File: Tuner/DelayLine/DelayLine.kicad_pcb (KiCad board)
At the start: 2 copper layers, 100 x 100 mm, 85 parts, among them J1 Conn_Coaxial, J10 Conn_Coaxial, J11 Conn_Coaxial, J12 Conn_Coaxial, J13 Conn_01x01, J14 Conn_01x01, J15 Conn_01x01, J16 Conn_01x01, J17 Conn_02x10_Odd_Even, J18 Conn_Coaxial, J19 Conn_Coaxial, J20 Conn_Coaxial, J21 Conn_Coaxial, J22 Conn_Coaxial, J23 Conn_Coaxial, J24 Conn_01x01, J25 Conn_01x01, J26 Conn_01x01, J27 Conn_01x01, J28 Conn_01x01, J29 Conn_Coaxial, J3 Conn_Coaxial, J31 Conn_Coaxial, J32 Conn_01x01, J33 Conn_01x01, J34 Conn_01x01, J35 Conn_01x01, J5 Conn_Coaxial, J6 Conn_Coaxial, J7 Conn_Coaxial, J8 Conn_01x02, J9 Conn_01x02

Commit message: Stupid mistake, went to another method
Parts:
- moved J19 3.63 mm to (116.6, 107.1)
- moved J6 2.70 mm to (124.1, 119.0)
- moved J12 2.59 mm to (108.6, 119.3)
- moved J10 2.48 mm to (131.8, 106.8)
- moved J23 2.46 mm to (100.0, 106.8)
- moved J29 1.78 mm to (75.1, 119.0)
- moved J21 1.75 mm to (92.0, 119.1)
- moved J31 1.63 mm to (83.5, 106.9)
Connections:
- J22 pad 1: Net-(J11-Pad1) -> Net-(J22-Pad1)
- J23 pad 1: Net-(J12-Pad1) -> Net-(J23-Pad1)
- J24 pad 1: Net-(J20-Pad1) -> Net-(J24-Pad1)
- J3 pad 1: Net-(J29-Pad1) -> Net-(J3-Pad1)
- J31 pad 1: Net-(J21-Pad1) -> Net-(J31-Pad1)
- J5 pad 1: Net-(J18-Pad1) -> Net-(J5-Pad1)
- J6 pad 1: Net-(J19-Pad1) -> Net-(J6-Pad1)
- J7 pad 1: Net-(J1-Pad1) -> Net-(J7-Pad1)
- RLY1 pad 4: Net-(J10-Pad1) -> Net-(RLY1-Pad4)
- RLY1 pad 8: Net-(J10-Pad1) -> Net-(RLY1-Pad4)
- RLY10 pad 3: Net-(J20-Pad1) -> Net-(J24-Pad1)
- RLY10 pad 7: Net-(J20-Pad1) -> (no net)
- RLY2 pad 2: Net-(J10-Pad1) -> Net-(RLY2-Pad2)
- RLY2 pad 3: Net-(J19-Pad1) -> Net-(RLY2-Pad3)
- RLY2 pad 4: (no net) -> Net-(J6-Pad1)
- RLY2 pad 6: Net-(J10-Pad1) -> Net-(RLY1-Pad4)
- RLY2 pad 7: Net-(J19-Pad1) -> Net-(RLY2-Pad3)
- RLY2 pad 8: (no net) -> Net-(J10-Pad1)
- RLY3 pad 2: Net-(J19-Pad1) -> Net-(RLY3-Pad2)
- RLY3 pad 3: Net-(J12-Pad1) -> Net-(RLY3-Pad3)
- RLY3 pad 4: (no net) -> Net-(J12-Pad1)
- RLY3 pad 6: Net-(J19-Pad1) -> Net-(RLY2-Pad2)
- RLY3 pad 7: Net-(J12-Pad1) -> Net-(RLY3-Pad3)
- RLY3 pad 8: (no net) -> Net-(J19-Pad1)
- RLY4 pad 2: Net-(J12-Pad1) -> Net-(RLY4-Pad2)
- RLY4 pad 3: Net-(J21-Pad1) -> Net-(RLY4-Pad3)
- RLY4 pad 4: (no net) -> Net-(J21-Pad1)
- RLY4 pad 6: Net-(J12-Pad1) -> Net-(RLY3-Pad2)
- RLY4 pad 7: Net-(J21-Pad1) -> Net-(RLY4-Pad3)
- RLY4 pad 8: (no net) -> Net-(J23-Pad1)
- RLY5 pad 2: Net-(J21-Pad1) -> Net-(RLY5-Pad2)
- RLY5 pad 3: Net-(J29-Pad1) -> Net-(RLY5-Pad3)
- RLY5 pad 4: (no net) -> Net-(J29-Pad1)
- RLY5 pad 6: Net-(J21-Pad1) -> Net-(RLY4-Pad2)
- RLY5 pad 7: Net-(J29-Pad1) -> Net-(RLY5-Pad3)
- RLY5 pad 8: (no net) -> Net-(J31-Pad1)
- RLY6 pad 2: Net-(J29-Pad1) -> Net-(RLY6-Pad2)
- RLY6 pad 3: Net-(J1-Pad1) -> Net-(RLY6-Pad3)
- RLY6 pad 4: (no net) -> Net-(J1-Pad1)
- RLY6 pad 6: Net-(J29-Pad1) -> Net-(RLY5-Pad2)
- RLY6 pad 7: Net-(J1-Pad1) -> Net-(RLY6-Pad3)
- RLY6 pad 8: (no net) -> Net-(J3-Pad1)
- RLY7 pad 2: Net-(J1-Pad1) -> Net-(RLY7-Pad2)
- RLY7 pad 3: Net-(J18-Pad1) -> Net-(RLY7-Pad3)
- RLY7 pad 4: (no net) -> Net-(J5-Pad1)
- RLY7 pad 6: Net-(J1-Pad1) -> Net-(RLY6-Pad2)
- RLY7 pad 7: Net-(J18-Pad1) -> Net-(RLY7-Pad3)
- RLY7 pad 8: (no net) -> Net-(J7-Pad1)
- RLY8 pad 2: Net-(J18-Pad1) -> Net-(RLY8-Pad2)
- RLY8 pad 3: Net-(J11-Pad1) -> Net-(RLY8-Pad3)
- RLY8 pad 4: (no net) -> Net-(J11-Pad1)
- RLY8 pad 6: Net-(J18-Pad1) -> Net-(RLY7-Pad2)
- RLY8 pad 7: Net-(J11-Pad1) -> Net-(RLY8-Pad3)
- RLY8 pad 8: (no net) -> Net-(J18-Pad1)
- RLY9 pad 2: Net-(J11-Pad1) -> Net-(J24-Pad1)
- RLY9 pad 3: Net-(J20-Pad1) -> Net-(RLY9-Pad3)
- RLY9 pad 4: (no net) -> Net-(J20-Pad1)
- RLY9 pad 6: Net-(J11-Pad1) -> Net-(RLY8-Pad2)
- RLY9 pad 7: Net-(J20-Pad1) -> Net-(RLY9-Pad3)
- RLY9 pad 8: (no net) -> Net-(J22-Pad1)
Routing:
- net Net-(RLY5-Pad2): track 0.00 -> 79.9 mm
- net Net-(J29-Pad1): track 91.4 -> 12.5 mm
- net Net-(J1-Pad1): track 62.0 -> 8.69 mm
- net Net-(J11-Pad1): track 62.9 -> 9.88 mm
- net RFGND: track 906.3 -> 854.0 mm
- net Net-(J21-Pad1): track 60.1 -> 13.0 mm
- net Net-(J12-Pad1): track 58.6 -> 13.4 mm
- net Net-(J20-Pad1): track 53.3 -> 10.5 mm
- net Net-(J18-Pad1): track 62.7 -> 23.5 mm
- net Net-(J24-Pad1): track 0.00 -> 38.2 mm
- net Net-(J19-Pad1): track 59.0 -> 25.1 mm
- net Net-(J10-Pad1): track 49.5 -> 24.6 mm
- net Net-(J31-Pad1): track 0.00 -> 23.9 mm
- net Net-(J22-Pad1): track 0.00 -> 23.8 mm
- net Net-(J7-Pad1): track 0.00 -> 23.7 mm
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
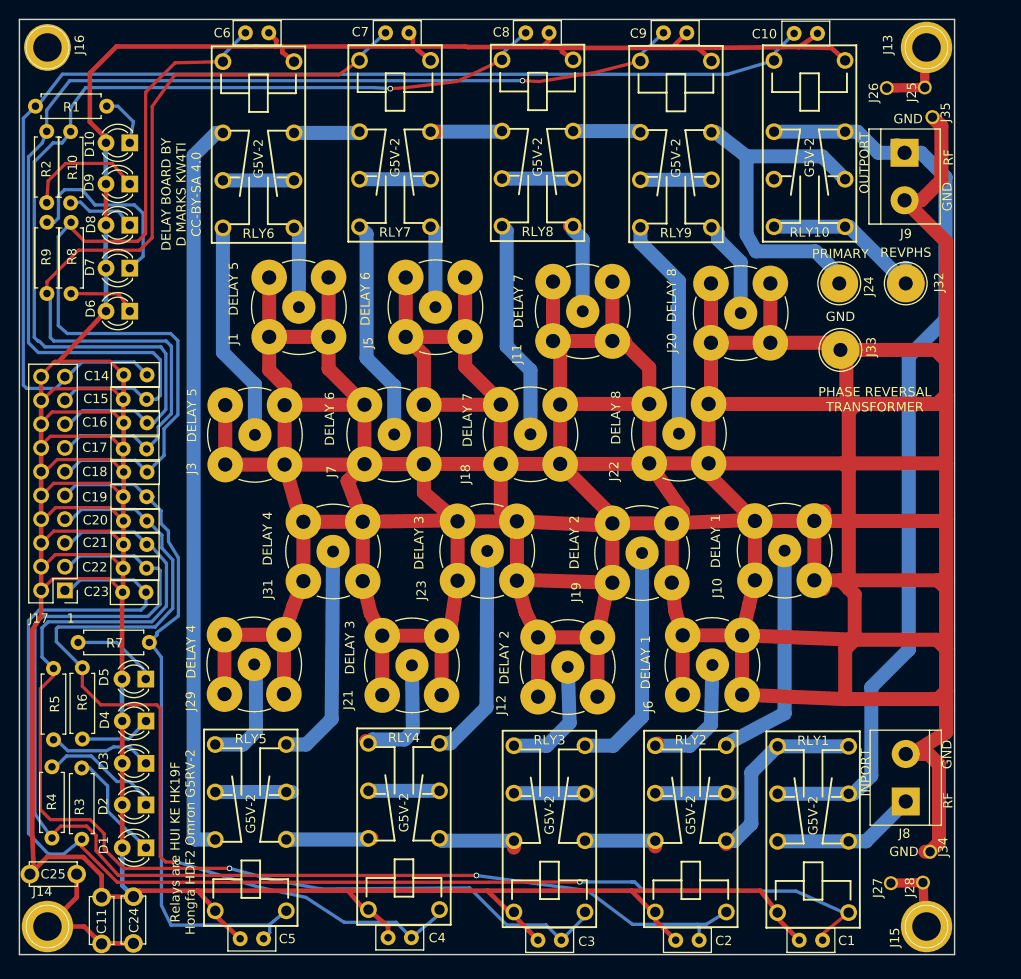
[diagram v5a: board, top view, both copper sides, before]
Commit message: Added LittleDelayLine
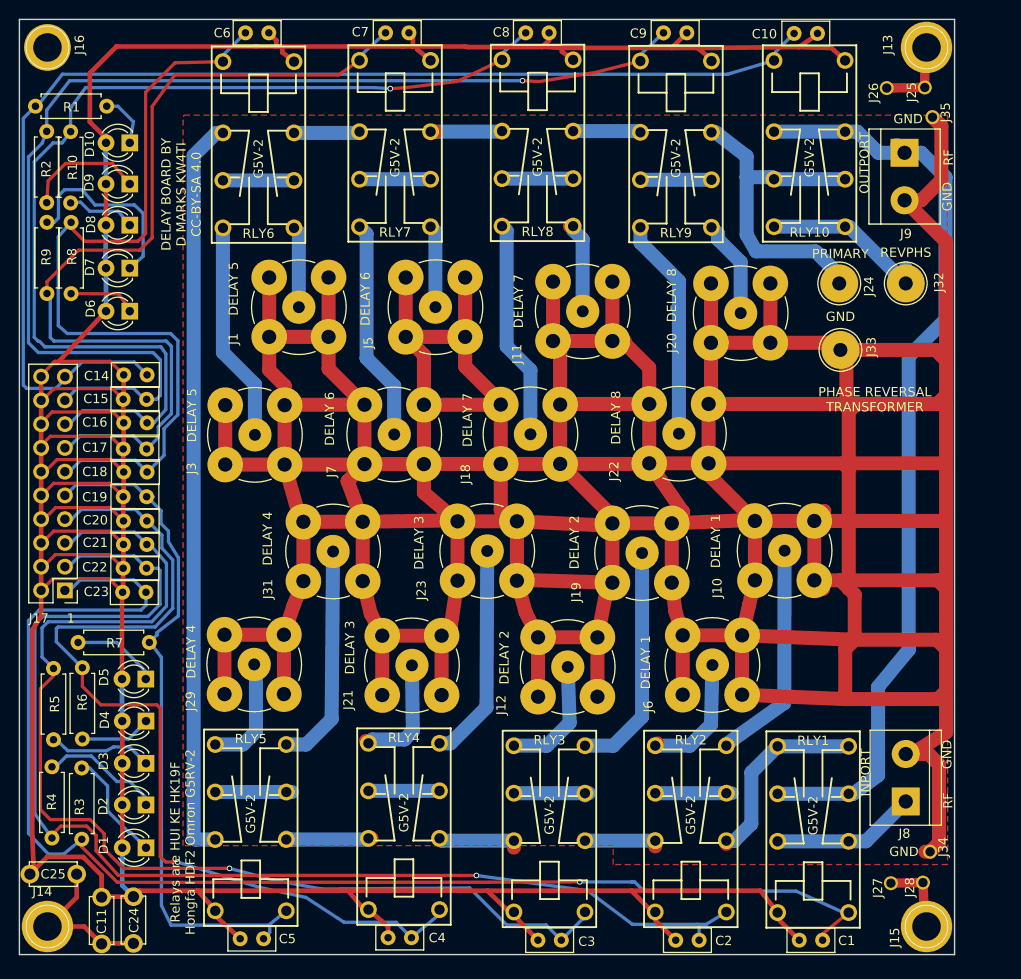
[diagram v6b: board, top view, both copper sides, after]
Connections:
- RLY10 pad 7: (no net) -> Net-(J24-Pad1)
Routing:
- net Net-(J24-Pad1): track 38.2 -> 37.3 mm
- net Net-(J10-Pad1): track 24.6 -> 24.0 mm
- added copper zone on F.Cu, net RFGND
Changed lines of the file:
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@@
 (kicad_pcb (version 4) (host pcbnew 4.0.7)
   (general
-    (links 220)
+    (links 221)
     (no_connects 0)
-    (area 49.924999 49.924999 150.075001 150.075001)
+    (area 44.941618 49.609999 151.74762 151.075)
     (thickness 1.6)
     (drawings 35)
-    (tracks 907)
+    (tracks 909)
     (zones 0)
     (modules 85)
@@
     (user_trace_width 1.5)
     (trace_clearance 0.2)
-    (zone_clearance 1.5)
+    (zone_clearance 1)
     (zone_45_only yes)
     (trace_min 0.2)
@@
     (pad 3 thru_hole circle (at 10.32 -3.8 270) (size 1.8 1.8) (drill 1.1) (layers *.Cu *.Mask)
       (net 52 "Net-(J24-Pad1)"))
-    (pad 7 thru_hole circle (at 10.32 3.8 270) (size 1.8 1.8) (drill 1.1) (layers *.Cu *.Mask))
+    (pad 7 thru_hole circle (at 10.32 3.8 270) (size 1.8 1.8) (drill 1.1) (layers *.Cu *.Mask)
+      (net 52 "Net-(J24-Pad1)"))
     (pad 6 thru_hole circle (at 5.24 3.8 270) (size 1.8 1.8) (drill 1.1) (layers *.Cu *.Mask)
       (net 37 RFOUT))
@@
   (segment (start 79.883 72.814) (end 79.365 72.296) (width 1.5) (layer B.Cu) (net 2))
   (segment (start 125.593 127.6655) (end 125.593 127.518) (width 1.5) (layer B.Cu) (net 3))
-  (segment (start 125.593 127.518) (end 131.826 124.2187) (width 1.5) (layer B.Cu) (net 3))
-  (segment (start 131.826 124.2187) (end 131.826 106.807) (width 1.5) (layer B.Cu) (net 3) (status 20))
+  (segment (start 125.593 127.518) (end 131.7879 123.1011) (width 1.5) (layer B.Cu) (net 3))
+  (segment (start 131.7879 123.1011) (end 131.826 106.807) (width 1.5) (layer B.Cu) (net 3) (status 800020))
   (segment (start 115.481152 142.237678) (end 115.796278 142.237678) (width 0.35) (layer B.Cu) (net 4))
   (segment (start 116.7765 143.2179) (end 133.056967 143.2179) (width 0.35) (layer B.Cu) (net 4))
@@
   (segment (start 138.674 132.809) (end 131.074 132.809) (width 1.5) (layer B.Cu) (net 37))
   (segment (start 138.674 132.809) (end 139.1615 132.809) (width 1.5) (layer B.Cu) (net 37))
-  (segment (start 139.1615 132.809) (end 141.097 130.8735) (width 1.5) (layer B.Cu) (net 37))
-  (segment (start 141.097 130.8735) (end 141.097 121.412) (width 1.5) (layer B.Cu) (net 37))
-  (segment (start 141.097 121.412) (end 145.0975 117.4115) (width 1.5) (layer B.Cu) (net 37))
+  (segment (start 139.1615 132.809) (end 141.8209 130.8481) (width 1.5) (layer B.Cu) (net 37))
+  (segment (start 141.8209 130.8481) (end 141.8209 121.3866) (width 1.5) (layer B.Cu) (net 37))
+  (segment (start 141.8209 121.3866) (end 145.0975 117.4115) (width 1.5) (layer B.Cu) (net 37))
   (segment (start 145.0975 117.4115) (end 145.0975 86.0425) (width 1.5) (layer B.Cu) (net 37))
   (segment (start 145.0975 86.0425) (end 149.0345 82.1055) (width 1.5) (layer B.Cu) (net 37))
@@
   (segment (start 94.488 80.772) (end 94.488 72.687) (width 1.5) (layer B.Cu) (net 51))
   (segment (start 94.488 72.687) (end 93.97 72.169) (width 1.5) (layer B.Cu) (net 51))
+  (segment (start 127.762 66.8655) (end 130.4695 66.8655) (width 1.5) (layer B.Cu) (net 52))
+  (segment (start 130.4695 66.8655) (end 130.693 67.089) (width 1.5) (layer B.Cu) (net 52))
+  (segment (start 138.293 67.089) (end 130.693 67.089) (width 1.5) (layer B.Cu) (net 52))
   (segment (start 137.668 78.232) (end 137.668 77.343) (width 1.5) (layer B.Cu) (net 52))
   (segment (start 137.668 77.343) (end 135.128 74.803) (width 1.5) (layer B.Cu) (net 52))
-  (segment (start 127.762 73.025) (end 127.762 64.643) (width 1.5) (layer B.Cu) (net 52))
+  (segment (start 127.762 73.025) (end 127.762 66.8655) (width 1.5) (layer B.Cu) (net 52))
+  (segment (start 127.762 66.8655) (end 127.762 64.643) (width 1.5) (layer B.Cu) (net 52))
   (segment (start 128.778 74.803) (end 127.762 73.025) (width 1.5) (layer B.Cu) (net 52))
   (segment (start 135.128 74.803) (end 128.778 74.803) (width 1.5) (layer B.Cu) (net 52))
   (segment (start 124.0055 62.0725) (end 124.4295 62.0725) (width 1.5) (layer B.Cu) (net 52))
   (segment (start 124.4295 62.0725) (end 127.762 64.643) (width 1.5) (layer B.Cu) (net 52))
-  (segment (start 135.847 64.643) (end 138.293 67.089) (width 1.5) (layer B.Cu) (net 52))
-  (segment (start 127.762 64.643) (end 135.847 64.643) (width 1.5) (layer B.Cu) (net 52))
   (segment (start 124.0055 62.0725) (end 124.2365 62.0725) (width 1.5) (layer F.Cu) (net 52))
   (segment (start 137.668 78.232) (end 137.668 77.851) (width 1.5) (layer B.Cu) (net 52))
@@
   (segment (start 123.952 119.1895) (end 124.1044 119.0371) (width 1.5) (layer B.Cu) (net 61) (status 30))
   (segment (start 118.237 127.4215) (end 117.993 127.6655) (width 1.5) (layer F.Cu) (net 61))
+  (zone (net 1) (net_name RFGND) (layer F.Cu) (hatch edge 0.508)
+    (connect_pads (clearance 1))
+    (min_thickness 0.635)
+    (fill yes (arc_segments 16) (thermal_gap 0.508) (thermal_bridge_width 3))
+    (polygon
+      (pts
+        (xy 67.6148 60.2361) (xy 149.2504 60.2361) (xy 149.2504 140.3731) (xy 113.4872 140.3731) (xy 113.4872 138.3538)
+        (xy 67.5005 138.3538) (xy 67.5005 60.3504) (xy 67.6148 60.3504)
+      )
+    )
+  )
 )

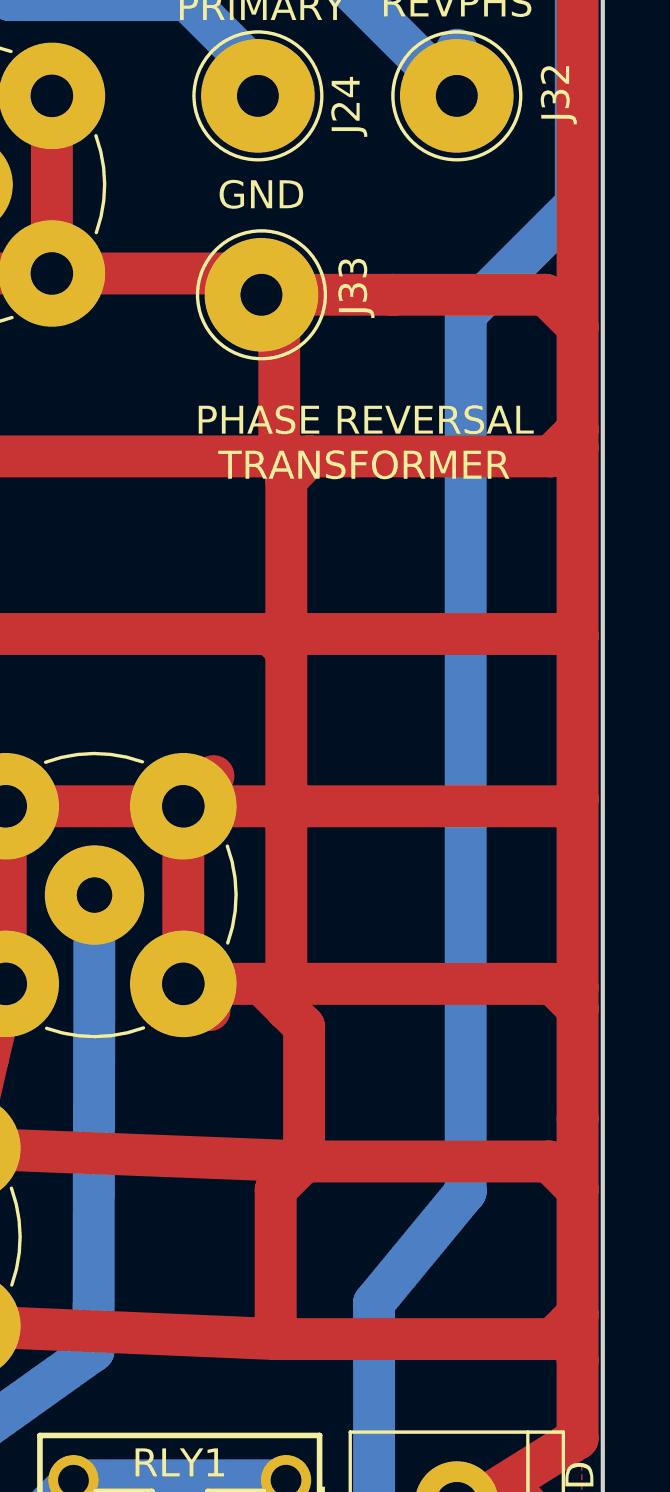
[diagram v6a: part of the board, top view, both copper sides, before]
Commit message: Added more instrumentation to TandemMatch, fixed grounding issue
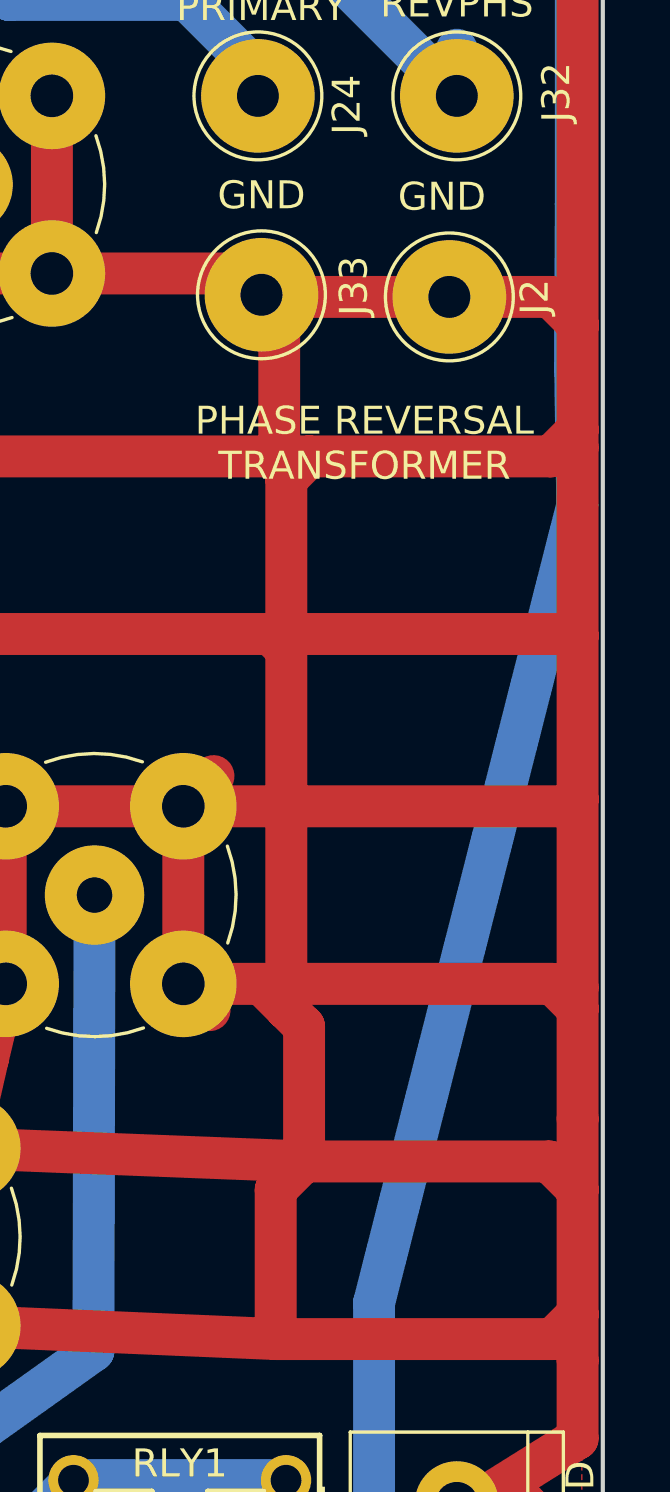
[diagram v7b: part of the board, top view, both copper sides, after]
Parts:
- added J2: Conn_01x01, Connectors:1pin, F.Cu at (144.5, 85.4)
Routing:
- net RFOUT: track 99.7 -> 97.8 mm
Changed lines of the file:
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@@
 (kicad_pcb (version 4) (host pcbnew 4.0.7)
   (general
-    (links 221)
+    (links 222)
     (no_connects 0)
-    (area 44.941618 49.609999 151.74762 151.075)
+    (area 49.924999 49.924999 150.075001 150.075001)
     (thickness 1.6)
-    (drawings 35)
-    (tracks 909)
+    (drawings 36)
+    (tracks 911)
     (zones 0)
-    (modules 85)
+    (modules 86)
     (nets 62)
   )
@@
       (net 1 RFGND))
   )
+  (module Connectors:1pin (layer F.Cu)
+    (at 144.5133 85.4202 270)
+    (descr "module 1 pin (ou trou mecanique de percage)")
+    (tags DEV)
+    (fp_text reference J2 (at 0 -3.048 270) (layer F.SilkS)
+      (effects (font (size 1 1) (thickness 0.15)))
+    )
+    (fp_text value Conn_01x01 (at 0 3 270) (layer F.Fab)
+      (effects (font (size 1 1) (thickness 0.15)))
+    )
+    (fp_circle (center 0 0) (end 2 0.8) (layer F.Fab) (width 0.1))
+    (fp_circle (center 0 0) (end 2.6 0) (layer F.CrtYd) (width 0.05))
+    (fp_circle (center 0 0) (end 0 -2.286) (layer F.SilkS) (width 0.12))
+    (pad 1 thru_hole circle (at 0 0 270) (size 4.064 4.064) (drill 1.5) (layers *.Cu *.Mask)
+      (net 1 RFGND))
+  )
+  (gr_text GND (at 144.2466 81.8388) (layer F.SilkS)
+    (effects (font (size 1 1) (thickness 0.15)))
+  )
   (gr_text GND (at 144.5895 139.0015) (layer F.SilkS)
     (effects (font (size 1 1) (thickness 0.15)))
@@
   (gr_line (start 150 150) (end 50 150) (angle 90) (layer Edge.Cuts) (width 0.15))
   (gr_line (start 50 50) (end 150 50) (angle 90) (layer Edge.Cuts) (width 0.15))
+  (segment (start 144.5133 85.4202) (end 148.1328 85.4202) (width 1.5) (layer F.Cu) (net 1))
+  (segment (start 148.1328 85.4202) (end 149.098 86.3854) (width 1.5) (layer F.Cu) (net 1))
+  (segment (start 144.5133 85.4202) (end 137.8712 85.4202) (width 1.5) (layer F.Cu) (net 1))
+  (segment (start 137.8712 85.4202) (end 137.795 85.344) (width 1.5) (layer F.Cu) (net 1))
   (segment (start 138.43 91.1225) (end 138.43 85.979) (width 1.5) (layer F.Cu) (net 1))
   (segment (start 138.43 85.979) (end 137.795 85.344) (width 1.5) (layer F.Cu) (net 1))
@@
   (segment (start 148.336 129.667) (end 148.336 138.049) (width 1.5) (layer F.Cu) (net 1))
   (segment (start 147.2184 128.5494) (end 148.336 129.667) (width 1.5) (layer F.Cu) (net 1))
-  (segment (start 137.795 85.344) (end 142.494 85.344) (width 1.5) (layer F.Cu) (net 1))
-  (segment (start 142.494 85.344) (end 147.955 85.344) (width 1.5) (layer F.Cu) (net 1))
-  (segment (start 147.955 85.344) (end 149.098 86.487) (width 1.5) (layer F.Cu) (net 1))
   (segment (start 144.78 128.5494) (end 145.4023 128.5494) (width 1.5) (layer F.Cu) (net 1) (status 30))
   (segment (start 145.4023 128.5494) (end 149.098 126.238) (width 1.5) (layer F.Cu) (net 1) (status 10))
@@
   (segment (start 149.098 97.536) (end 149.098 90.805) (width 1.5) (layer F.Cu) (net 1))
   (segment (start 149.098 90.805) (end 149.098 90.17) (width 1.5) (layer F.Cu) (net 1))
-  (segment (start 149.098 90.17) (end 149.098 86.487) (width 1.5) (layer F.Cu) (net 1))
-  (segment (start 149.098 73.787) (end 144.653 69.342) (width 1.5) (layer F.Cu) (net 1))
+  (segment (start 149.098 90.17) (end 149.098 86.3854) (width 1.5) (layer F.Cu) (net 1))
+  (segment (start 149.098 86.3854) (end 149.098 86.487) (width 1.5) (layer F.Cu) (net 1))
   (segment (start 149.098 86.487) (end 149.098 73.787) (width 1.5) (layer F.Cu) (net 1))
+  (segment (start 149.098 73.787) (end 144.653 69.342) (width 1.5) (layer F.Cu) (net 1))
   (segment (start 144.78 128.5494) (end 145.3896 128.5494) (width 1) (layer F.Cu) (net 1) (status 30))
   (segment (start 145.39468 70.08368) (end 144.653 69.342) (width 1.5) (layer F.Cu) (net 1) (status 30))
@@
   (segment (start 125.593 127.6655) (end 125.593 127.518) (width 1.5) (layer B.Cu) (net 3))
   (segment (start 125.593 127.518) (end 131.7879 123.1011) (width 1.5) (layer B.Cu) (net 3))
-  (segment (start 131.7879 123.1011) (end 131.826 106.807) (width 1.5) (layer B.Cu) (net 3) (status 800020))
+  (segment (start 131.7879 123.1011) (end 131.826 106.807) (width 1.5) (layer B.Cu) (net 3) (status 20))
   (segment (start 115.481152 142.237678) (end 115.796278 142.237678) (width 0.35) (layer B.Cu) (net 4))
   (segment (start 116.7765 143.2179) (end 133.056967 143.2179) (width 0.35) (layer B.Cu) (net 4))
@@
   (segment (start 139.1615 132.809) (end 141.8209 130.8481) (width 1.5) (layer B.Cu) (net 37))
   (segment (start 141.8209 130.8481) (end 141.8209 121.3866) (width 1.5) (layer B.Cu) (net 37))
-  (segment (start 141.8209 121.3866) (end 145.0975 117.4115) (width 1.5) (layer B.Cu) (net 37))
-  (segment (start 145.0975 117.4115) (end 145.0975 86.0425) (width 1.5) (layer B.Cu) (net 37))
-  (segment (start 145.0975 86.0425) (end 149.0345 82.1055) (width 1.5) (layer B.Cu) (net 37))
+  (segment (start 141.8209 121.3866) (end 149.08784 92.87256) (width 1.5) (layer B.Cu) (net 37))
+  (segment (start 149.08784 92.87256) (end 149.0091 87.94242) (width 1.5) (layer B.Cu) (net 37))
+  (segment (start 149.0091 87.94242) (end 149.0345 82.1055) (width 1.5) (layer B.Cu) (net 37))
   (segment (start 149.0345 82.1055) (end 149.0345 66.8655) (width 1.5) (layer B.Cu) (net 37))
   (segment (start 149.0345 66.8655) (end 146.431 64.262) (width 1.5) (layer B.Cu) (net 37))
